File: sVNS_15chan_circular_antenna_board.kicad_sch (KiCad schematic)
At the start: 0 parts

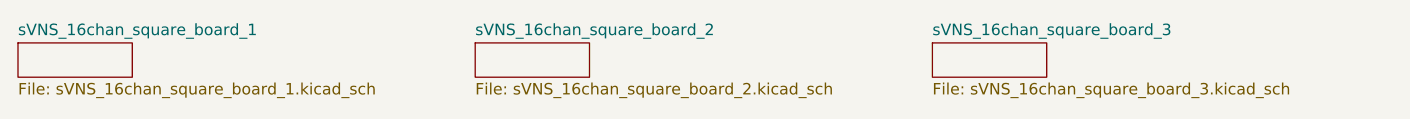
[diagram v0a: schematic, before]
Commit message: V1.2. Slightly modified the device schematic to align with Kicad perspective after import from Eagle.
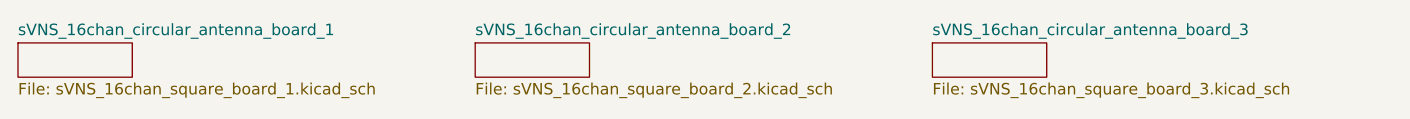
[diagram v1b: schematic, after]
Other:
- sheet sVNS_16chan_square_board_1 renamed sVNS_16chan_circular_antenna_board_1
- sheet sVNS_16chan_square_board_2 renamed sVNS_16chan_circular_antenna_board_2
- sheet sVNS_16chan_square_board_3 renamed sVNS_16chan_circular_antenna_board_3
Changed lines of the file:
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@@
 			(color 0 0 0 0)
 		)
-		(property "Sheetname" "sVNS_16chan_square_board_1"
+		(property "Sheetname" "sVNS_16chan_circular_antenna_board_1"
 			(at 25.4 24.6884 0)
 			(show_name no)
@@
 			(color 0 0 0 0)
 		)
-		(property "Sheetname" "sVNS_16chan_square_board_2"
+		(property "Sheetname" "sVNS_16chan_circular_antenna_board_2"
 			(at 76.2 24.6884 0)
 			(show_name no)
@@
 			(color 0 0 0 0)
 		)
-		(property "Sheetname" "sVNS_16chan_square_board_3"
+		(property "Sheetname" "sVNS_16chan_circular_antenna_board_3"
 			(at 127 24.6884 0)
 			(show_name no)

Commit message: V1.8. Preliminary layout of the grouped ICs and their discreted res/caps.
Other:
- note added: "Capacitor notes: choose X7R for the device, C0G/NP0 for the antenna tuning caps. For +3.3V X7R 0402 choose +10V voltage rating For +20V X7R 0402 choose +50V voltage rating"
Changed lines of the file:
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@@
 	(generator_version "10.0")
 	(paper "A4")
+	(text "Capacitor notes: choose X7R for the device, C0G/NP0 for the antenna tuning caps.\nFor +3.3V X7R 0402 choose +10V voltage rating\nFor +20V X7R 0402 choose +50V voltage rating"
+		(exclude_from_sim no)
+		(at 25.654 55.88 0)
+		(effects
+			(font
+				(size 1.27 1.27)
+			)
+			(justify left)
+		)
+	)
 	(sheet
 		(at 25.4 25.4)
